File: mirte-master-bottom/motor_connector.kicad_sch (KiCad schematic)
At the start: 9 parts, among them J8 Motor_conn, U4 DRV8231DDAR

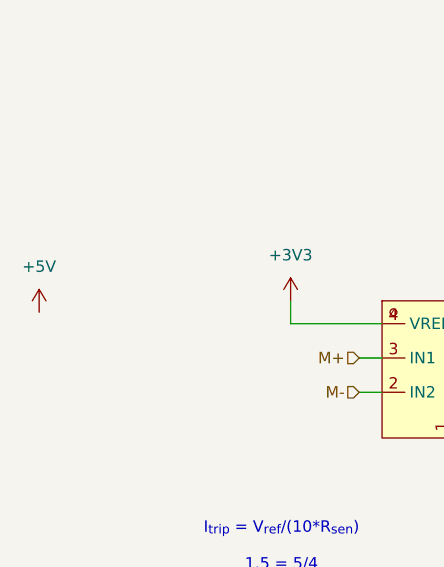
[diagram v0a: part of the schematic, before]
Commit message: MM: ERC&DRC fixes + change hbridge cap
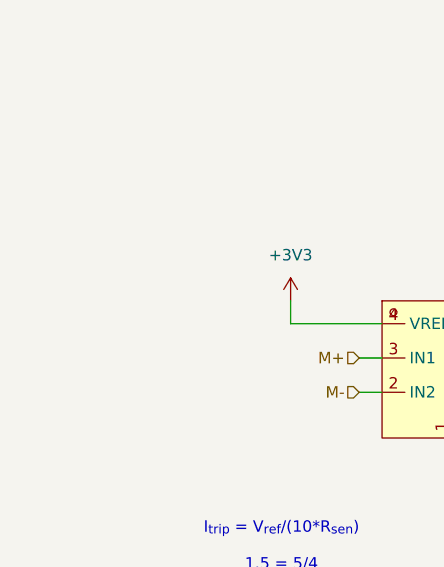
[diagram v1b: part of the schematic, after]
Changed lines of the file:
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@@
-	)
-	(symbol
-		(lib_id "power:+5V")
-		(at 11.43 72.39 0)
-		(unit 1)
-		(exclude_from_sim no)
-		(in_bom yes)
-		(on_board yes)
-		(dnp no)
-		(fields_autoplaced yes)
-		(property "Reference" "#PWR111"
-			(at 11.43 76.2 0)
-			(effects
-				(font
-					(size 1.27 1.27)
-				)
-				(hide yes)
-			)
-		)
-		(property "Value" "+5V"
-			(at 11.43 67.31 0)
-			(effects
-				(font
-					(size 1.27 1.27)
-				)
-			)
-		)
-		(property "Footprint" ""
-			(at 11.43 72.39 0)
-			(effects
-				(font
-					(size 1.27 1.27)
-				)
-				(hide yes)
-			)
-		)
-		(property "Datasheet" ""
-			(at 11.43 72.39 0)
-			(effects
-				(font
-					(size 1.27 1.27)
-				)
-				(hide yes)
-			)
-		)
-		(property "Description" "Power symbol creates a global label with name \"+5V\""
-			(at 11.43 72.39 0)
-			(effects
-				(font
-					(size 1.27 1.27)
-				)
-				(hide yes)
-			)
-		)
-		(pin "1"
-		)
-		(instances
-			(project "mirte-master-bottom"
-				(path "/c479422a-501d-4123-8665-56a1c70bd9ea/15e76074-7fdd-433c-b518-bfaad427cf18/b9602611-d294-41a3-a7d4-5d870159613d"
-					(reference "#PWR111")
-					(unit 1)
-				)
-				(path "/c479422a-501d-4123-8665-56a1c70bd9ea/15e76074-7fdd-433c-b518-bfaad427cf18/c9e28398-488a-47c9-85fd-446a05f82831"
-					(reference "#PWR112")
-					(unit 1)
-				)
-			)
-		)
 	)
 	(symbol

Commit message: MM: order big
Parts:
- C19: LCSC (none) -> C3349
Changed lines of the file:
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@@
+			)
+		)
+		(property "LCSC" "C3349"
+			(at 93.98 57.8149 0)
+			(effects
+				(font
+					(size 1.27 1.27)
+				)
+				(hide yes)
 			)
 		)
